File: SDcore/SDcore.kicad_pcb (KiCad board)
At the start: 4 copper layers, 24 x 32 mm, 44 parts, among them J1 SD_Card_Device, Q1 L2N7002WT1G, U1 RP2350A_C42411118, U2 NMUX27518EPWJ, U3 W25Q128JVEIQ_TR, X1 ABM8-272-T3_C20625731

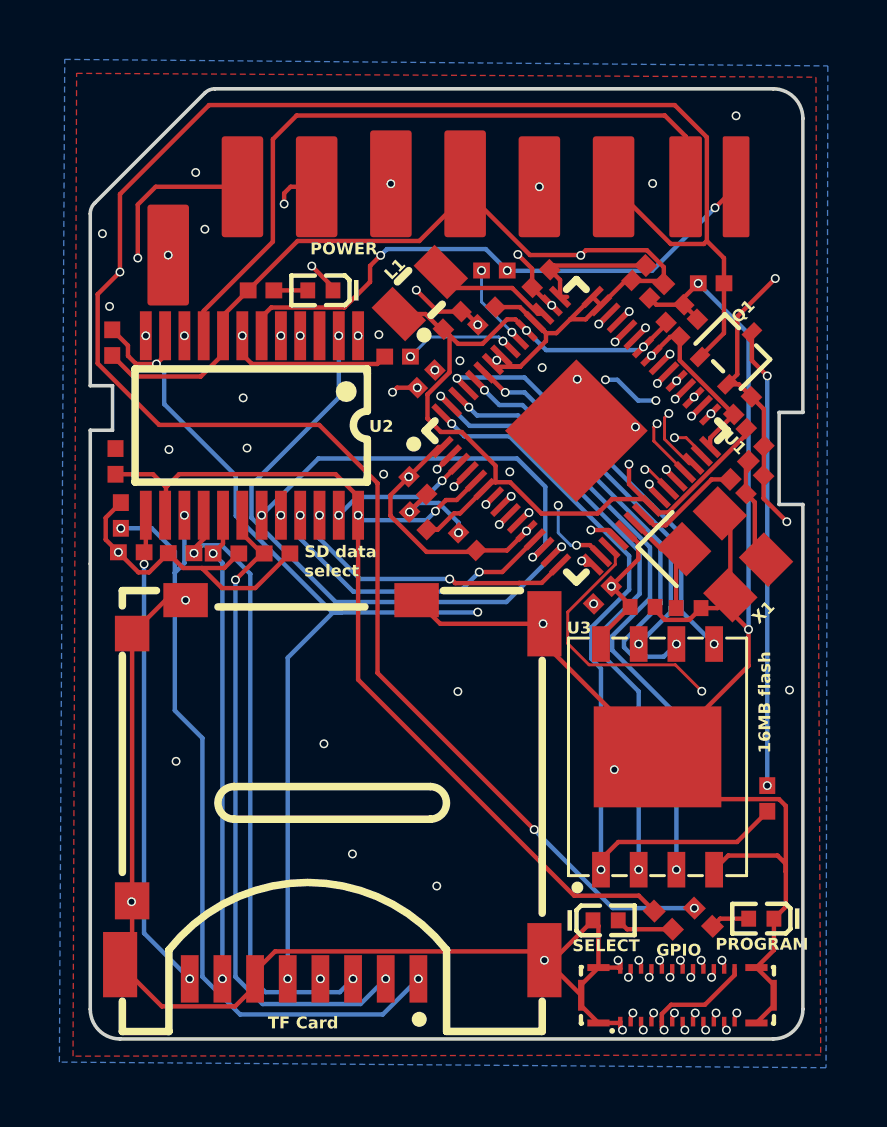
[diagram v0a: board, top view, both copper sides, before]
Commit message: Added clearings on the side like an actual SD card
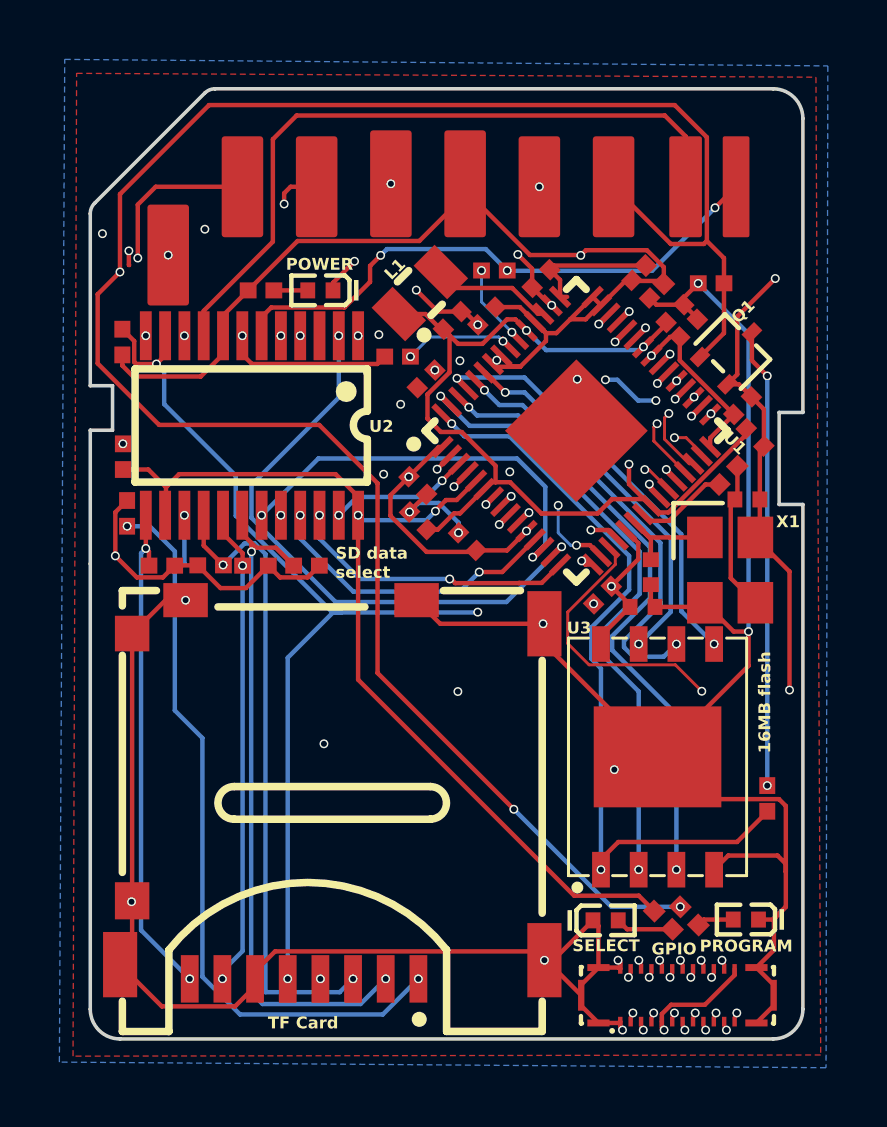
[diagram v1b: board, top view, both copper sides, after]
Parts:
- moved C15 1.75 mm to (177.2, 92.6), turned to -90 degrees
- moved R16 1.12 mm to (160.8, 92.4), turned to 0 degrees
- moved R12 1.07 mm to (165.6, 92.4)
- moved R13 1.07 mm to (162.4, 92.3)
- moved R15 1.07 mm to (163.9, 92.4)
- moved C14 0.56 mm to (180.5, 90.1), turned to 180 degrees
- moved X1 0.56 mm to (179.9, 92.5), turned to -90 degrees
- moved LED2 0.52 mm to (180.4, 104.3)
- moved R9 0.48 mm to (178.5, 104.2)
- moved R6 0.41 mm to (179.8, 89.3)
- moved R14 0.34 mm to (159.4, 84.8)
- moved R7 0.30 mm to (159.4, 88.7)
- moved R11 0.22 mm to (159.6, 90.6)
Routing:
- net GND: track 150.7 -> 154.6 mm, vias 45 -> 33
- net Net-(C14-Pad2): track 3.63 -> 5.25 mm
- net XIN: track 4.14 -> 5.56 mm
- net DATA_SD_SNIFF_1: track 38.7 -> 39.3 mm
- net XOUT: track 3.73 -> 3.17 mm
- net OUT_DAT0: track 25.8 -> 25.2 mm
